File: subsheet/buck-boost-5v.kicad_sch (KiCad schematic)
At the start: 11 parts, among them U1101 TPS563201

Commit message: Replace buck-regulator with buck-boost regulator
Replaced the buck-regulator with a buck-boost regulator. The primary
purpose is because the buck-regulator could fail when a higher-voltage
output was conected. The buck-regulators internal switches and design
should be much less vulnerable for this.

A second benefit of the buck-boost regulator is thata 5V input can now
still be used, as it accounts for the voltage-drop from the
bridge-rectifier diodes.
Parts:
- removed C1101, C1102: 10uF/25v, Capacitor_SMD:C_0805_2012Metric, symbol Device:C_Small
- removed C1103: 100nF, Capacitor_SMD:C_0603_1608Metric, symbol Device:C_Small
- removed C? (x4): 10uF/10V, Capacitor_SMD:C_0603_1608Metric, symbol Device:C_Small
- removed L1101: 3.3uH/1.2mΩ, Inductor_SMD:L_Sunlord_MWSA0402S, symbol Device:L
- removed R1101: 56kΩ/1%, Resistor_SMD:R_0603_1608Metric, symbol Device:R_Small_US
- removed R1102: 10kΩ/1%, Resistor_SMD:R_0603_1608Metric, symbol Device:R_Small_US
- removed U1101: TPS563201, Package_TO_SOT_SMD:SOT-23-6, symbol Regulator_Switching:TPS563200
- added C1004, C1005, C1006, C1007: 10uF/10V, Capacitor_SMD:C_0603_1608Metric, symbol Device:C_Small
- added C1010, C1011: 10uF/25v, Capacitor_SMD:C_0805_2012Metric, symbol Device:C_Small
- added C1012: 100nF, Capacitor_SMD:C_0603_1608Metric, symbol Device:C_Small
- added L1003: 1.5uH, Inductor_SMD:L_Changjiang_FNR252012S, symbol Device:L
- added R1003: 100kΩ, Resistor_SMD:R_0603_1608Metric, symbol Device:R_Small_US
- added R1004: 680kΩ, Resistor_SMD:R_0603_1608Metric, symbol Device:R_Small_US
- added R1005: 130kΩ, Resistor_SMD:R_0603_1608Metric, symbol Device:R_Small_US
- added U1002: TPS63070, symbol Regulator_Switching_custom:TPS63070
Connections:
- net 5v: now also C1004.1, C1005.1, C1006.1, C1007.1, R1004.1, U1002.7 (VOUT), U1002.8 (VOUT)
- net GND: now also C1004.2, C1005.2, C1006.2, C1007.2, C1010.2, C1011.2, C1012.2, R1005.2, U1002.10 (PGND), U1002.4 (GND)
- new net: R1004.2, R1005.1, U1002.5 (FB)
- new net: C1012.1, U1002.3 (VAUX)
- new net: R1003.2, U1002.1 (PS/SYNC), U1002.14 (EN)
- new net: L1003.1, U1002.11 (L1)
- new net: L1003.2, U1002.9 (L2)
- new net V_{IN}: C1010.1, C1011.1, R1003.1, U1002.12 (VIN), U1002.13 (VIN)
- no-connect marks 0 -> 2
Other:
- note removed: "I_{OUT} | eff. | I_{IN} 0.5A | 95% | 0.22A 1.0A | 95% | 0.45A 2.0A | 94% | 0.9A 3.0A | 92% | 1.38A @ 11.8V 3.0A | 92% | 1.55A @ 10.5V Keep that in mind when budgeting the 12V rail."
- note removed: "Max V_{IN} = 17V"
- note removed: "Note: Be careful about how close the Boot capacitor and FB resistor are to each other! If the high-frequency switching couples from BOOT to the FB pin, it will mess up the voltage regulation I encountered this while tesing v4.0.0: I touched them with my (dry) fingertip, causing an AC short between BOOT the FB pins on the resistors. The inductor would buzz, and board would stop working after 2 or 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"
- note removed: "Using WeBEnch circuit designer 5v - 3A output (same results for 1A) "Balanced""
- note removed: "When selecting inductor, consider max current AND saturation current I_{PEAK} = I_{MAX} + (I_{RIPPLE} / 2) = 3A + 0.5*1.5A = 3.75A"
- company: copyright Escape This 2024 -> (none)
- title: Puzzle Board -> (none)

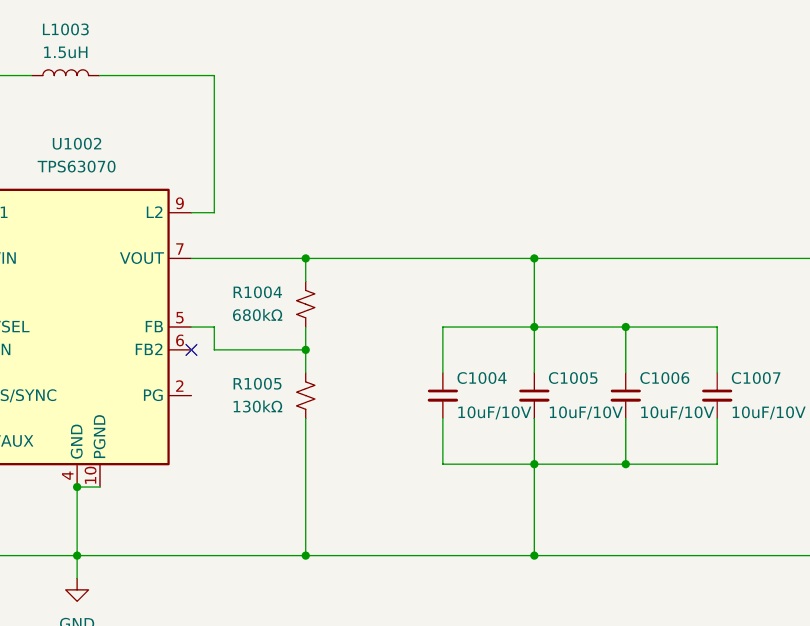
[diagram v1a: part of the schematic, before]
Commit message: Removed complex OR'ing circuit
Replaced it with a simple one that will turn off the USB 5V switch when
the buck-regulator is providing power (using PGOOD pin to signal this).

May not even be necessary, but good to have.
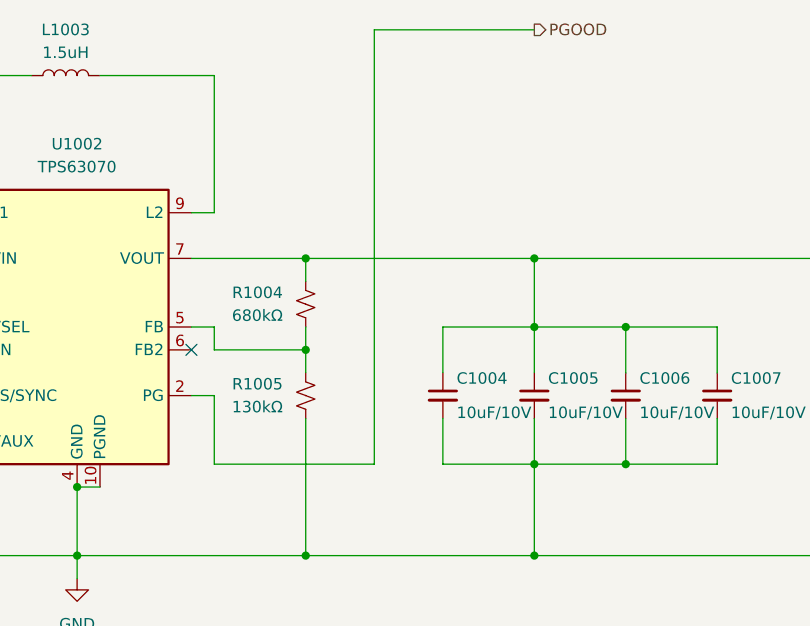
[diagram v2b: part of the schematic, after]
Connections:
- net PGOOD: now reaches U1002.2 (PG)
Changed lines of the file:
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@@
+	(wire
+		(pts
+			(xy 144.78 66.04) (xy 162.56 66.04)
+		)
+		(stroke
+			(width 0)
+			(type default)
+		)
+	)
 	(wire
 		(pts
@@
 	(wire
 		(pts
+			(xy 127 114.3) (xy 144.78 114.3)
+		)
+		(stroke
+			(width 0)
+			(type default)
+		)
+	)
+	(wire
+		(pts
 			(xy 127 71.12) (xy 127 86.36)
 		)
@@
 	(wire
 		(pts
+			(xy 127 106.68) (xy 127 114.3)
+		)
+		(stroke
+			(width 0)
+			(type default)
+		)
+	)
+	(wire
+		(pts
 			(xy 162.56 99.06) (xy 172.72 99.06)
 		)
@@
 	(wire
 		(pts
+			(xy 124.46 106.68) (xy 127 106.68)
+		)
+		(stroke
+			(width 0)
+			(type default)
+		)
+	)
+	(wire
+		(pts
 			(xy 91.44 91.44) (xy 91.44 93.98)
+		)
+		(stroke
+			(width 0)
+			(type default)
+		)
+	)
+	(wire
+		(pts
+			(xy 144.78 114.3) (xy 144.78 66.04)
 		)
 		(stroke
@@
 		)
 	)
+	(hierarchical_label "PGOOD"
+		(shape output)
+		(at 162.56 66.04 0)
+		(fields_autoplaced yes)
+		(effects
+			(font
+				(size 1.27 1.27)
+			)
+			(justify left)
+		)
+	)

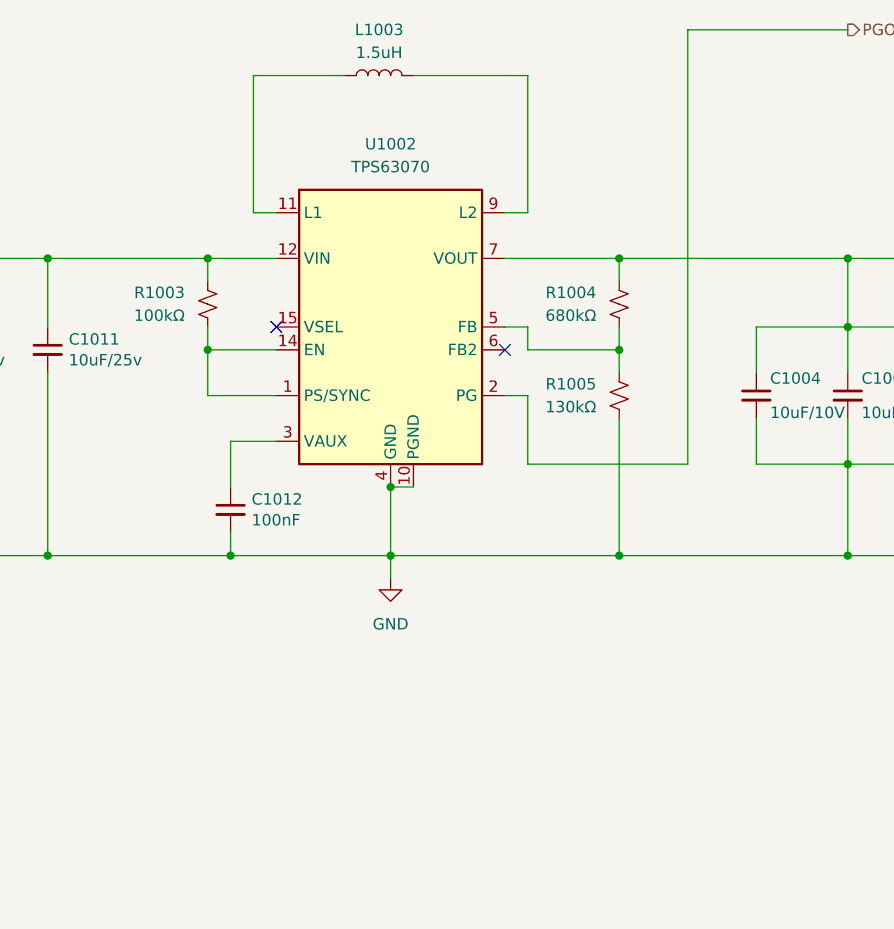
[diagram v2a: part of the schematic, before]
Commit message: Arranged buck-boost regulator. Moved some components slightly.
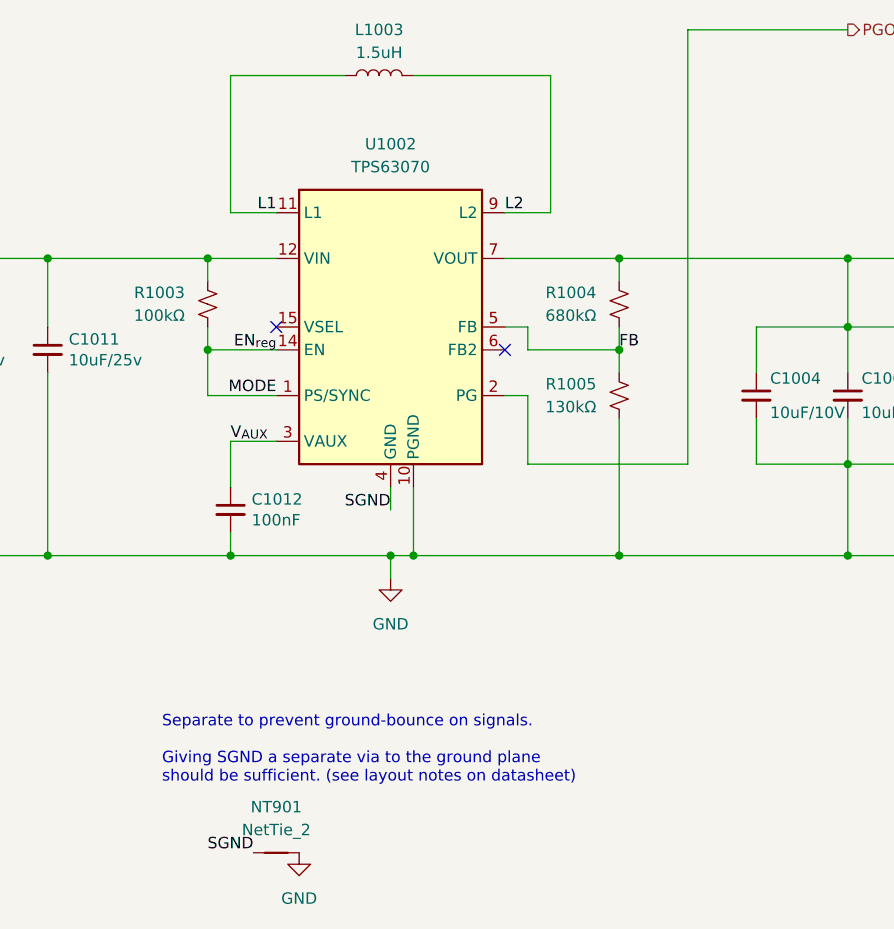
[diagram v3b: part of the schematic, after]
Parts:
- added NT901: NetTie_2, symbol Device:NetTie_2
- U1002: footprint (none) -> Package_DFN_QFN_custom:VQFN-15-HR_2.5x3mm_P0.5mm
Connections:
- net GND: now also NT901.2; no longer U1002.4 (GND)
- net FB: now reaches R1004.2, R1005.1, U1002.5 (FB)
- net V_{AUX}: now reaches C1012.1, U1002.3 (VAUX)
- net EN_{reg}: now reaches R1003.2, U1002.1 (PS/SYNC), U1002.14 (EN)
- net L1: now reaches L1003.1, U1002.11 (L1)
- net L2: now reaches L1003.2, U1002.9 (L2)
- new net SGND: NT901.1, U1002.4 (GND)
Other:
- note added: "Separate to prevent ground-bounce on signals. Giving SGND a separate via to the ground plane should be sufficient. (see layout notes on datasheet)"

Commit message: Layed-out 5V buck-boost regulator ciruit
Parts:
- C1010, C1011: footprint Capacitor_SMD:C_0805_2012Metric -> Capacitor_SMD:C_0603_1608Metric; LCSC C15850 -> C96446
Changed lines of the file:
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@@
 			)
 		)
-		(property "Footprint" "Capacitor_SMD:C_0805_2012Metric"
+		(property "Footprint" "Capacitor_SMD:C_0603_1608Metric"
 			(at 73.66 101.6 0)
 			(effects
@@
 			)
 		)
-		(property "LCSC" "C15850"
+		(property "LCSC" "C96446"
 			(at 73.66 101.6 0)
 			(effects
@@
 			)
 		)
-		(property "Footprint" "Capacitor_SMD:C_0805_2012Metric"
+		(property "Footprint" "Capacitor_SMD:C_0603_1608Metric"
 			(at 58.42 101.6 0)
 			(effects
@@
 			)
 		)
-		(property "LCSC" "C15850"
+		(property "LCSC" "C96446"
 			(at 58.42 101.6 0)
 			(effects

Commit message: Position final few components
Removed one ESD diode arrray - experimental board, so not really needed,
with the exception of the USB lines.

Add and position 5V indicator LED

Finished wiring up the 5V buck-boost regulator
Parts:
- NT901: footprint (none) -> NetTie:NetTie-2_SMD_Pad0.5mm
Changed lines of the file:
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@@
 			)
 		)
-		(property "Footprint" ""
+		(property "Footprint" "NetTie:NetTie-2_SMD_Pad0.5mm"
 			(at 99.06 157.48 0)
 			(effects

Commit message: Add order codes for all components
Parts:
- NT901: JLCPCB_IGNORE (none) -> 1
- R1004: LCSC (none) -> C25822
- R1005: LCSC (none) -> C22795
- U1002: LCSC (none) -> C109322
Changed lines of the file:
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@@
+			)
+		)
+		(property "I2C address" ""
+			(at 73.66 101.6 0)
+			(effects
+				(font
+					(size 1.27 1.27)
+				)
+				(hide yes)
 			)
 		)
@@
 			)
 		)
-		(property "LCSC" ""
+		(property "LCSC" "C25822"
 			(at 137.16 96.52 90)
+			(effects
+				(font
+					(size 1.27 1.27)
+				)
+				(hide yes)
+			)
+		)
+		(property "I2C address" ""
+			(at 137.16 96.52 0)
 			(effects
 				(font
@@
 		)
 		(property "LCSC" "C19702"
+			(at 152.4 106.68 0)
+			(effects
+				(font
+					(size 1.27 1.27)
+				)
+				(hide yes)
+			)
+		)
+		(property "I2C address" ""
 			(at 152.4 106.68 0)
 			(effects
@@
 			)
 		)
-		(property "LCSC" ""
+		(property "LCSC" "C22795"
 			(at 137.16 106.68 90)
+			(effects
+				(font
+					(size 1.27 1.27)
+				)
+				(hide yes)
+			)
+		)
+		(property "I2C address" ""
+			(at 137.16 106.68 0)
 			(effects
 				(font
@@
 			)
 		)
+		(property "I2C address" ""
+			(at 99.06 157.48 0)
+			(effects
+				(font
+					(size 1.27 1.27)
+				)
+				(hide yes)
+			)
+		)
+		(property "JLCPCB_IGNORE" "1"
+			(at 99.06 157.48 0)
+			(effects
+				(font
+					(size 1.27 1.27)
+				)
+				(hide yes)
+			)
+		)
 		(pin "2"
 		)
@@
 		)
 		(property "LCSC" "C96446"
+			(at 58.42 101.6 0)
+			(effects
+				(font
+					(size 1.27 1.27)
+				)
+				(hide yes)
+			)
+		)
+		(property "I2C address" ""
 			(at 58.42 101.6 0)
 			(effects
@@
 			)
 		)
+		(property "I2C address" ""
+			(at 93.98 119.38 0)
+			(effects
+				(font
+					(size 1.27 1.27)
+				)
+				(hide yes)
+			)
+		)
 		(pin "1"
 		)
@@
 			)
 		)
+		(property "I2C address" ""
+			(at 111.76 99.06 0)
+			(effects
+				(font
+					(size 1.27 1.27)
+				)
+				(hide yes)
+			)
+		)
+		(property "LCSC" "C109322"
+			(at 111.76 99.06 0)
+			(effects
+				(font
+					(size 1.27 1.27)
+				)
+				(hide yes)
+			)
+		)
 		(pin "5"
 		)
@@
 			)
 		)
+		(property "I2C address" ""
+			(at 91.44 96.52 0)
+			(effects
+				(font
+					(size 1.27 1.27)
+				)
+				(hide yes)
+			)
+		)
 		(pin "1"
 		)
@@
 			)
 		)
+		(property "I2C address" ""
+			(at 110.49 71.12 0)
+			(effects
+				(font
+					(size 1.27 1.27)
+				)
+				(hide yes)
+			)
+		)
 		(pin "1"
 		)
@@
 		)
 		(property "LCSC" "C19702"
+			(at 172.72 106.68 0)
+			(effects
+				(font
+					(size 1.27 1.27)
+				)
+				(hide yes)
+			)
+		)
+		(property "I2C address" ""
 			(at 172.72 106.68 0)
 			(effects
@@
 			)
 		)
+		(property "I2C address" ""
+			(at 162.56 106.68 0)
+			(effects
+				(font
+					(size 1.27 1.27)
+				)
+				(hide yes)
+			)
+		)
 		(pin "1"
 		)
@@
 			(at 182.88 106.68 0)
 			(effects
+				(font
+					(size 1.27 1.27)
+				)
+				(hide yes)
+			)
+		)
+		(property "I2C address" ""
+			(at 182.88 106.68 0)
+			(effects

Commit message: Silkscreen work. Edit tittle block/version number
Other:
- company: (none) -> (c) Vincent Dalstra
- title: (none) -> Untitled 4-layer JLCPCB
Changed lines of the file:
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@@
 	(generator_version "8.0")
 	(paper "A4")
+	(title_block
+		(title "Untitled 4-layer JLCPCB")
+		(date "2024-06-14")
+		(rev "1.0.0")
+		(company "(c) Vincent Dalstra")
+	)
 	(junction
 		(at 137.16 101.6)

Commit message: Final corrections and silkscreen labels
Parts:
- U1002: JLCPCB_CORRECTION (none) -> 0;0;270
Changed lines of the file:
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@@
+			)
+		)
+		(property "JLCPCB_CORRECTION" "0;0;270"
+			(at 111.76 99.06 0)
+			(effects
+				(font
+					(size 1.27 1.27)
+				)
+				(hide yes)
 			)
 		)
